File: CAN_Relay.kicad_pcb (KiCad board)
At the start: 2 copper layers, 86.4 x 86.4 mm, 28 parts, among them IC1 REG1117-5, J1 430450601, J2 BCS-114-L-S-PE-BE, J3 BCS-114-L-S-PE-BE, J4 691305340008, J5 691305340008, U2 BTS716GB, U3 BTS716GB, U4 ADM3057EBRWZ

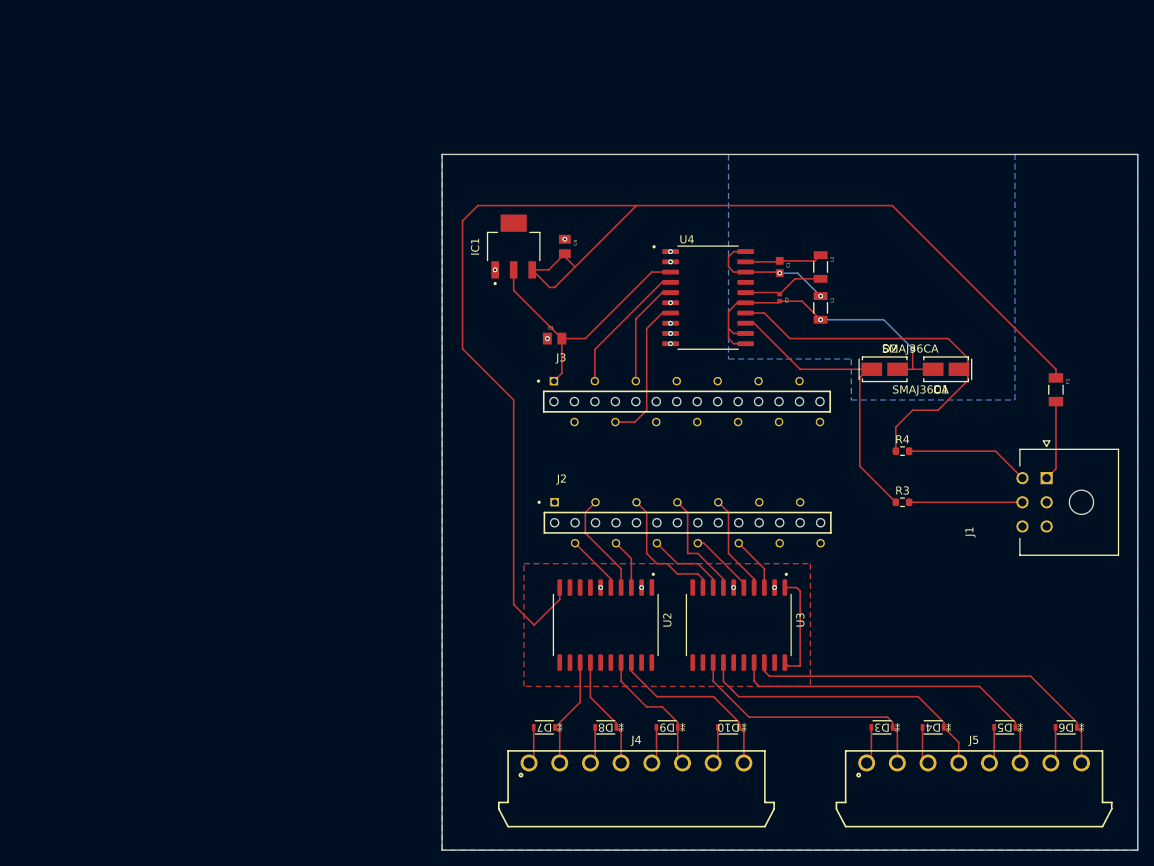
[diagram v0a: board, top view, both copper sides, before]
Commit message: Redid layout to make board more compact
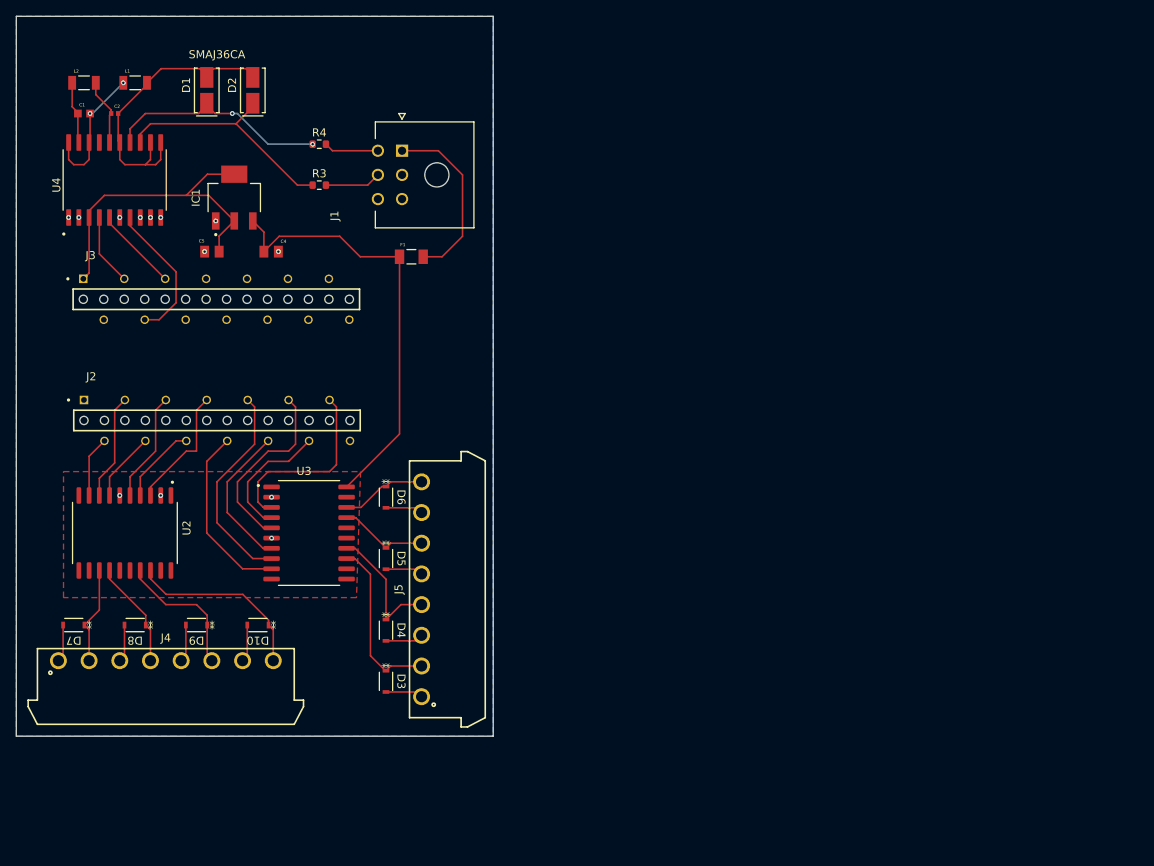
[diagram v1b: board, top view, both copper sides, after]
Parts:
- moved D1 98.1 mm to (62.2, 58.1), turned to 90 degrees
- moved L2 94.3 mm to (47.0, 57.1), turned to 0 degrees
- moved J1 89.7 mm to (86.5, 65.6)
- moved L1 89.6 mm to (53.3, 57.1), turned to 0 degrees
- moved D6 89.1 mm to (84.5, 108.6), turned to -90 degrees
- moved C1 88.4 mm to (47.0, 61.0), turned to 0 degrees
- moved D2 85.7 mm to (67.9, 58.1), turned to 90 degrees
- moved C2 85.7 mm to (50.8, 61.0), turned to 0 degrees
- moved R3 82.4 mm to (76.2, 69.8)
- moved R4 81.8 mm to (76.2, 64.8)
- moved F1 81.7 mm to (87.6, 78.7), turned to 0 degrees
- moved D5 79.6 mm to (84.5, 116.2), turned to -90 degrees
- moved U4 75.1 mm to (50.8, 69.2), turned to 90 degrees
- moved J5 71.9 mm to (88.9, 120.0), turned to 90 degrees
- moved D4 69.0 mm to (84.5, 125.1), turned to -90 degrees
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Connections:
- J2 pad 02: Net-(U2-IN2) -> Net-(U2-IN4)
- J2 pad 03: Net-(U2-ST1/2) -> Net-(U2-ST3/4)
- J2 pad 04: Net-(U2-IN1) -> Net-(U2-IN3)
- J2 pad 05: Net-(U3-IN4) -> Net-(U2-IN2)
- J2 pad 06: Net-(U3-ST3/4) -> Net-(U2-ST1/2)
- J2 pad 07: Net-(U3-IN3) -> Net-(U2-IN1)
- J2 pad 08: Net-(U3-IN2) -> Net-(U3-IN4)
- J2 pad 09: Net-(U3-ST1/2) -> Net-(U3-ST3/4)
- J2 pad 10: Net-(U3-IN1) -> Net-(U3-IN3)
- J2 pad 11: unconnected-(J2-Pad11) -> Net-(U3-IN2)
- J2 pad 12: unconnected-(J2-Pad12) -> Net-(U3-ST1/2)
- J2 pad 13: unconnected-(J2-Pad13) -> Net-(U3-IN1)
- U2 pad 7: unconnected-(U2-IN3-Pad7) -> Net-(U2-IN3)
- U2 pad 8: unconnected-(U2-ST3/4-Pad8) -> Net-(U2-ST3/4)
- U2 pad 9: unconnected-(U2-IN4-Pad9) -> Net-(U2-IN4)
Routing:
- net +12: track 182.3 -> 54.4 mm
- net Net-(D6-K): track 47.8 -> 10.6 mm
- net Net-(D5-K): track 42.2 -> 11.1 mm
- net Net-(D4-K): track 37.6 -> 16.7 mm
- net /CaNHi: track 47.9 -> 27.8 mm, vias 0 -> 2
- net Net-(U3-IN1): track 6.82 -> 23.5 mm
- net Net-(U3-ST3/4): track 9.89 -> 26.1 mm
- net Net-(U3-IN2): track 8.31 -> 23.1 mm
- net Net-(U2-ST3/4): track 0.00 -> 13.2 mm
- net Net-(F1-Pad2): track 9.98 -> 22.3 mm
- net Net-(D3-K): track 32.0 -> 21.3 mm
- net Net-(U2-IN1): track 6.29 -> 15.5 mm
- net /CaNH: track 15.5 -> 6.79 mm
- net Net-(U2-IN3): track 0.00 -> 8.62 mm
- net +3.3: track 16.8 -> 8.89 mm
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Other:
- board size 86.4 x 86.4 mm -> 59.2 x 89.4 mm
